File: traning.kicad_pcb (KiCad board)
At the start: 2 copper layers, 40.6 x 45.7 mm, 11 parts, among them J1 Conn_01x04_Socket, Q1 2SC1815, Q2 2SC1815

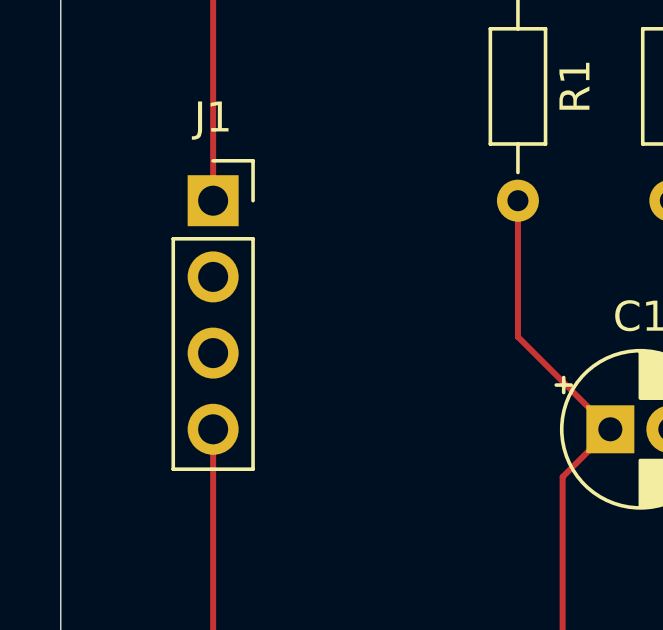
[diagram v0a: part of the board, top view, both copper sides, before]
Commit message: 未配線箇所を配線
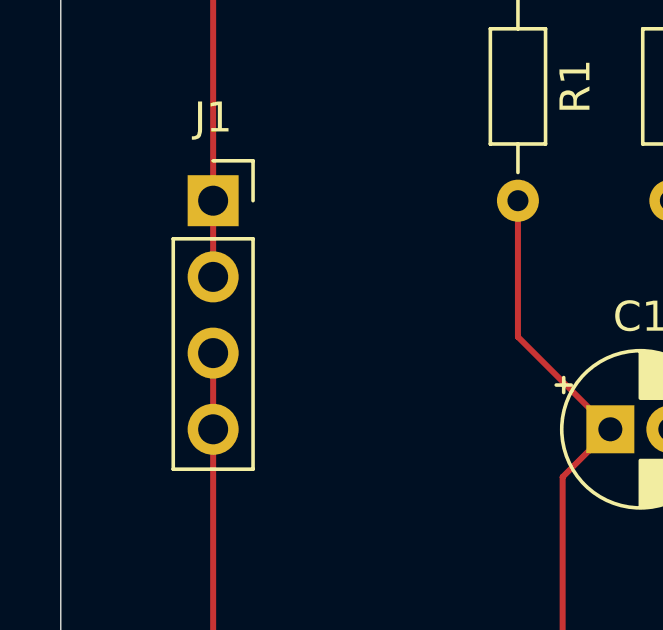
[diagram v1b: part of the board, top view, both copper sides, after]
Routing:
- net +5V: track 68.6 -> 71.1 mm
- net GND: track 43.2 -> 45.7 mm
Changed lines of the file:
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@@
 		(tags "CP Radial series Radial pin pitch 2.00mm  diameter 5mm Electrolytic Capacitor")
 		(property "Reference" "C2"
-			(at 1 -3.75 360)
+			(at 1 -3.75 0)
 			(layer "F.SilkS")
 			(effects
@@
 		)
 		(property "Value" "C"
-			(at 1 3.75 360)
+			(at 1 3.75 0)
 			(layer "F.Fab")
 			(effects
@@
 		)
 		(fp_text user "${REFERENCE}"
-			(at 1 0 360)
+			(at 1 0 0)
 			(layer "F.Fab")
 			(effects
@@
 	)
 	(segment
+		(start 119.38 81.28)
+		(end 119.38 78.74)
+		(width 0.2)
+		(layer "F.Cu")
+		(net 5)
+	)
+	(segment
 		(start 129.54 60.96)
 		(end 134.62 60.96)
@@
 		(width 0.2)
 		(layer "F.Cu")
+		(net 8)
+	)
+	(segment
+		(start 119.38 83.82)
+		(end 119.38 86.36)
+		(width 0.2)
+		(layer "F.Cu")

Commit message: 配線を修正
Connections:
- C2 pad 1: Net-(Q1-B) -> Net-(Q2-C)
- C2 pad 2: Net-(Q2-C) -> Net-(Q1-B)
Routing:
- net Net-(Q2-C): track 25.2 -> 19.9 mm
- net Net-(Q1-B): track 27.1 -> 25.4 mm
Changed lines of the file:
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@@
 			(layers "*.Cu" "*.Mask")
 			(remove_unused_layers no)
-			(net 4 "Net-(Q1-B)")
+			(net 3 "Net-(Q2-C)")
 			(pintype "passive")
 		)
@@
 			(layers "*.Cu" "*.Mask")
 			(remove_unused_layers no)
-			(net 3 "Net-(Q2-C)")
+			(net 4 "Net-(Q1-B)")
 			(pintype "passive")
 		)
@@
 	)
 	(segment
-		(start 148.42 87.46)
-		(end 145.88 87.46)
+		(start 149.86 83.82)
+		(end 147.32 86.36)
 		(width 0.2)
 		(layer "F.Cu")
@@
 	)
 	(segment
-		(start 145.88 87.46)
-		(end 145.32 86.9)
+		(start 149.86 78.74)
+		(end 149.86 83.82)
 		(width 0.2)
 		(layer "F.Cu")
@@
 	)
 	(segment
-		(start 145.32 91.98)
+		(start 147.32 93.98)
+		(end 147.32 86.36)
+		(width 0.2)
+		(layer "F.Cu")
+		(net 3)
+	)
+	(segment
+		(start 149.86 96.52)
+		(end 147.32 93.98)
+		(width 0.2)
+		(layer "F.Cu")
+		(net 3)
+	)
+	(segment
+		(start 144.78 78.74)
+		(end 144.78 85.82)
+		(width 0.2)
+		(layer "F.Cu")
+		(net 4)
+	)
+	(segment
+		(start 144.78 85.82)
 		(end 145.32 86.36)
 		(width 0.2)
 		(layer "F.Cu")
-		(net 3)
-	)
-	(segment
-		(start 145.32 86.9)
-		(end 145.32 86.36)
-		(width 0.2)
-		(layer "F.Cu")
-		(net 3)
-	)
-	(segment
-		(start 149.86 96.52)
-		(end 145.32 91.98)
-		(width 0.2)
-		(layer "F.Cu")
-		(net 3)
-	)
-	(segment
-		(start 149.86 78.74)
-		(end 149.86 86.02)
-		(width 0.2)
-		(layer "F.Cu")
-		(net 3)
-	)
-	(segment
-		(start 149.86 86.02)
-		(end 148.42 87.46)
-		(width 0.2)
-		(layer "F.Cu")
-		(net 3)
-	)
-	(segment
-		(start 144.78 83.82)
-		(end 147.32 86.36)
-		(width 0.2)
-		(layer "F.Cu")
 		(net 4)
 	)
 	(segment
-		(start 144.78 78.74)
-		(end 144.78 83.82)
-		(width 0.2)
-		(layer "F.Cu")
-		(net 4)
-	)
-	(segment
 		(start 139.7 93.98)
-		(end 147.32 86.36)
+		(end 145.32 88.36)
 		(width 0.2)
 		(layer "B.Cu")
@@
 		(width 0.2)
 		(layer "B.Cu")
+		(net 4)
+	)
+	(segment
+		(start 145.32 88.36)
+		(end 145.32 86.36)
+		(width 0.2)
+		(layer "B.Cu")
